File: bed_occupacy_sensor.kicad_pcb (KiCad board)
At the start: 2 copper layers, 48 x 34 mm, 6 parts, among them J1 FSR_2, J2 FSR_1, U1 mini_esp32

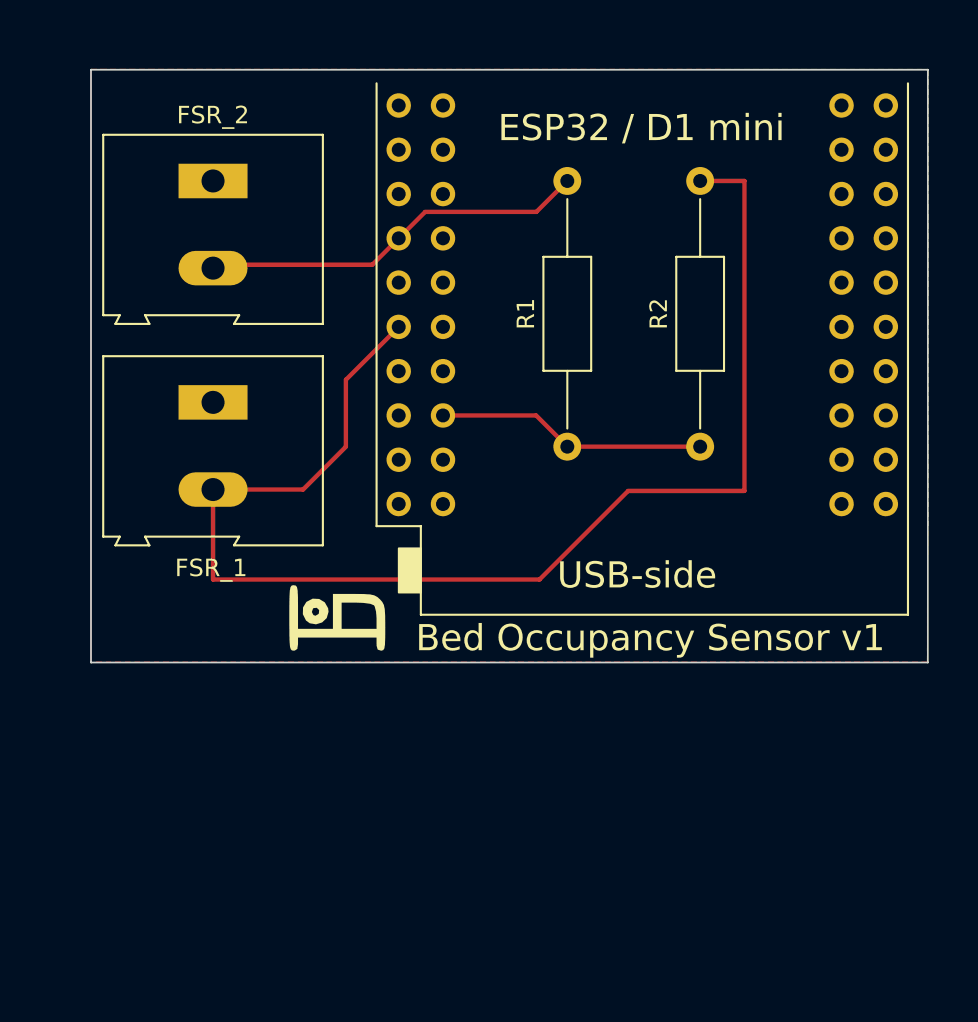
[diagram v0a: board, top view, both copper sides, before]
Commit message: Updated to design ESP32 flipped to get smaller PCB added QR-Code for Project-Link
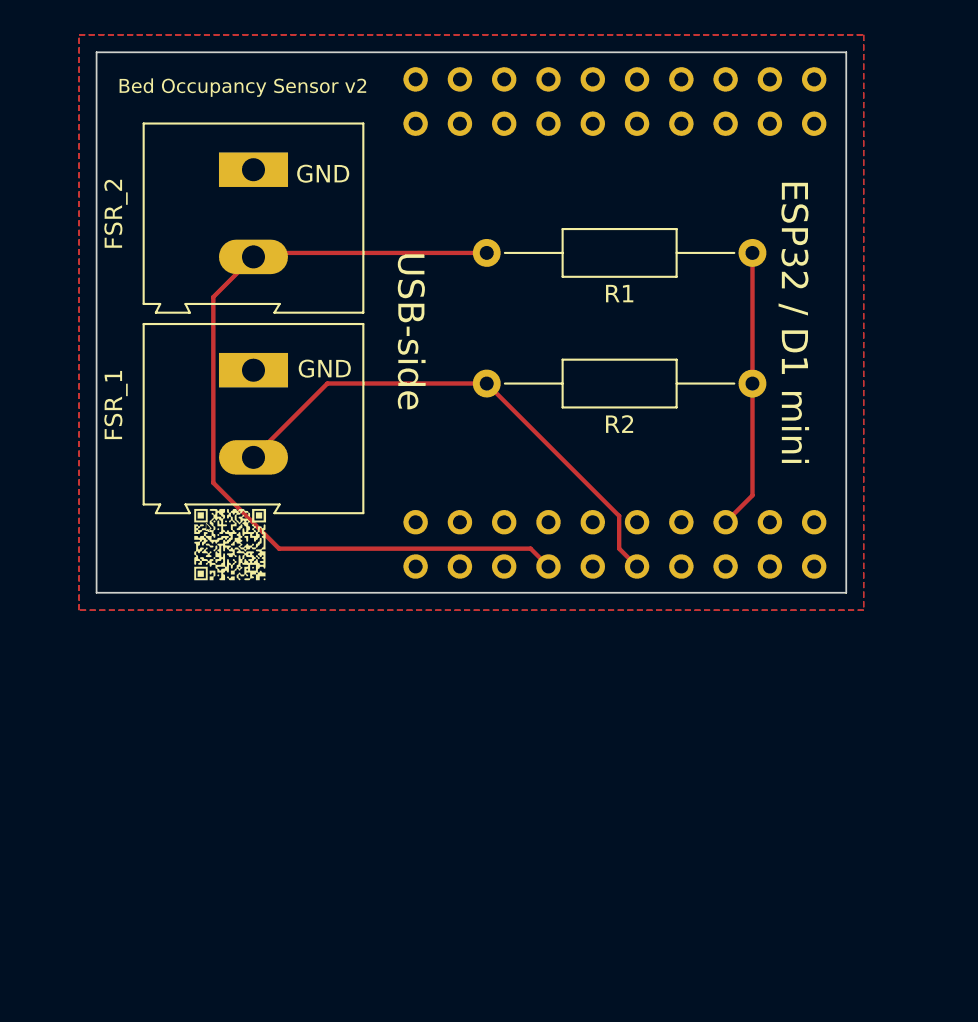
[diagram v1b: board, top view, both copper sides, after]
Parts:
- removed the G*** at (171.8, 123.3)
- added G***: LOGO, LOGO, F.Cu at (165.7, 119.2)
- moved R1 15.4 mm to (195.6, 102.5), turned to 180 degrees
- moved R2 4.70 mm to (195.6, 110.0), turned to 180 degrees
- moved J2 2.96 mm to (167.0, 109.2)
- moved J1 2.41 mm to (167.0, 97.7)
- moved U1 1.89 mm to (187.7, 106.5), turned to 90 degrees
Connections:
- net /GND renamed GND
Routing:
- net /SIDE_B: track 74.8 -> 29.2 mm
- net /SIDE_A: track 22.4 -> 48.6 mm
- net /+3V3: track 15.5 -> 16.1 mm
- added copper zone on B.Cu, net GND
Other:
- board size 48 x 34 mm -> 43 x 31 mm
- board text added: "Bed Occupancy Sensor v2"
- board text added: "GND"
- board text removed: "Bed Occupancy Sensor v1"

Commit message: complete redesign added terminal-block for getting power from external powersupply flipped esp header for getting smaller kicad_pcb added descriptions for pins and QR code
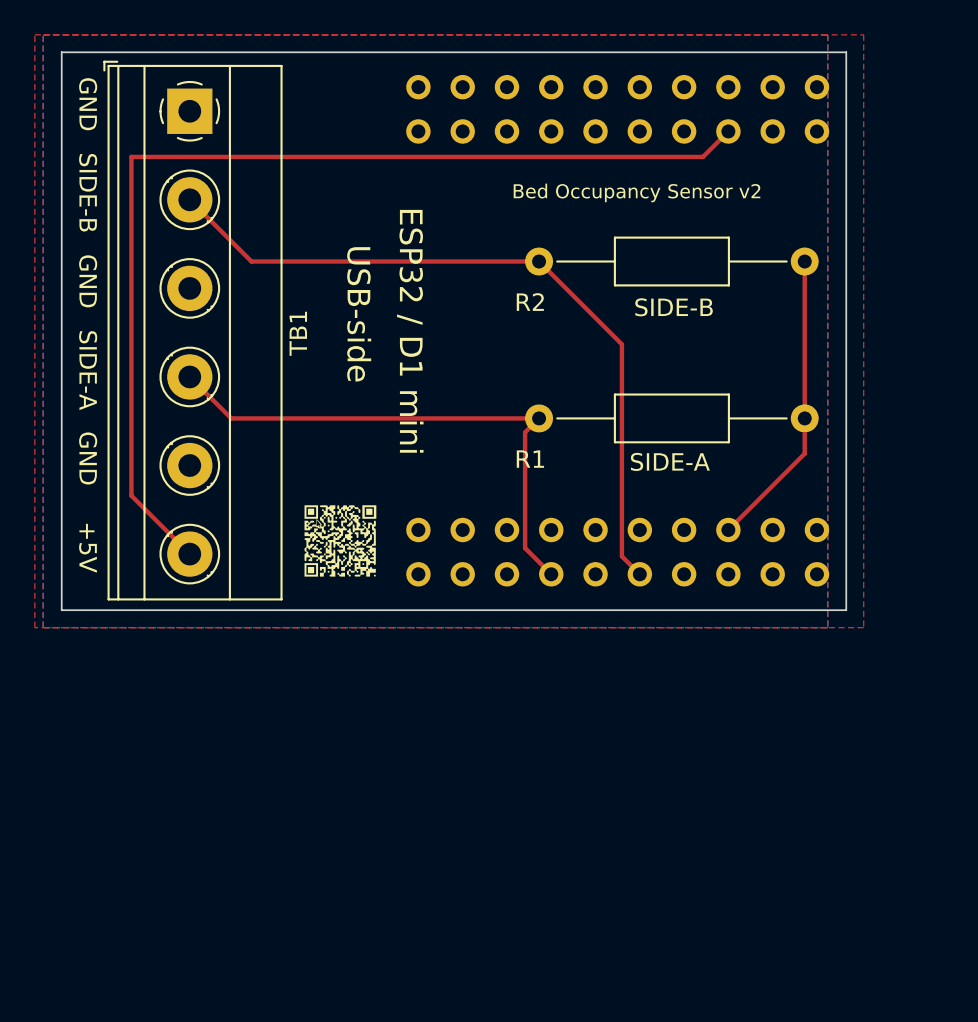
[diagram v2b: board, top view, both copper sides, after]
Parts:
- removed J1: FSR_2, TerminalBlock:TerminalBlock_Altech_AK300-2_P5.00mm
- removed J2: FSR_1, TerminalBlock:TerminalBlock_Altech_AK300-2_P5.00mm
- added TB1: 1729160, TerminalBlock_Phoenix:TerminalBlock_Phoenix_MKDS-1,5-6-5.08_1x06_P5.08mm_Horizontal, F.Cu at (163.3, 94.4)
- moved R1 9.96 mm to (198.6, 112.0)
- moved R2 7.62 mm to (198.6, 103.0)
- moved G*** 6.33 mm to (172.0, 119.0)
- moved U1 0.47 mm to (187.9, 107.0)
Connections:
- U1 pad 1: GND -> unconnected-(U1-Pad1)
- U1 pad 33: GND -> unconnected-(U1-Pad33)
- U1 pad 35: unconnected-(U1-Pad35) -> /VCC
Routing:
- net /VCC: track 0.00 -> 59.0 mm
- net /SIDE_A: track 48.6 -> 30.9 mm
- net /SIDE_B: track 29.2 -> 41.8 mm
- net /+3V3: track 16.1 -> 17.2 mm
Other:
- board size 43 x 31 mm -> 45 x 32 mm
- board text added: "+5V"
- board text added: "SIDE-A"
- board text added: "SIDE-B"

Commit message: Reverse the footprint of ESP, as it was the wrong way around
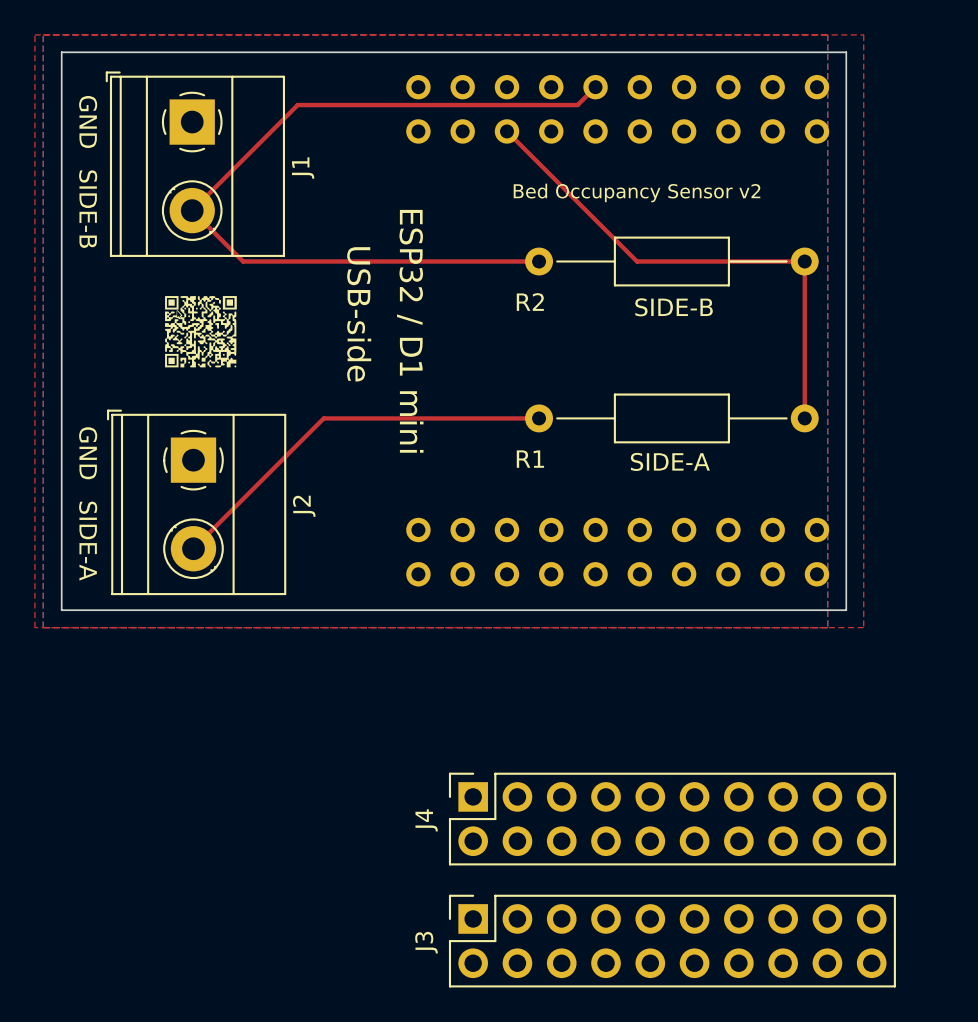
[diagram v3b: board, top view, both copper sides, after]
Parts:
- removed TB1: 1729160, TerminalBlock_Phoenix:TerminalBlock_Phoenix_MKDS-1,5-6-5.08_1x06_P5.08mm_Horizontal
- added J1: Screw_Terminal_01x02, TerminalBlock_Phoenix:TerminalBlock_Phoenix_MKDS-1,5-2-5.08_1x02_P5.08mm_Horizontal, F.Cu at (163.5, 95.0)
- added J2: Screw_Terminal_01x02, TerminalBlock_Phoenix:TerminalBlock_Phoenix_MKDS-1,5-2-5.08_1x02_P5.08mm_Horizontal, F.Cu at (163.6, 114.4)
- added J3: Conn_02x10_Top_Bottom, Connector_PinSocket_2.54mm:PinSocket_2x10_P2.54mm_Vertical, F.Cu at (179.6, 140.7)
- added J4: Conn_02x10_Top_Bottom, Connector_PinSocket_2.54mm:PinSocket_2x10_P2.54mm_Vertical, F.Cu at (179.6, 133.7)
- moved G*** 14.4 mm to (164.0, 107.0)
- turned U1 to -90 degrees
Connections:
- net /+3V3 renamed Net-(R1-Pad1)
- U1 pad 35: /VCC -> unconnected-(U1-Pad35)
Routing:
- net /VCC: track 59.0 -> 0.00 mm
- net Net-(R1-Pad1): track 17.2 -> 29.2 mm
- net /SIDE_A: track 30.9 -> 22.9 mm
- net /SIDE_B: track 41.8 -> 47.2 mm
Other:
- board text removed: "+5V"

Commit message: fixed design flaw of ESP-Pin orientation (it was the wrong way around). Now the antenna is free (on it's downside) removed QR Code because it's too small to read by a QR-Code-Reader. Updated the resistor footprint to a smaller one (10,4mm) because it fits better to standard metal-film resistors
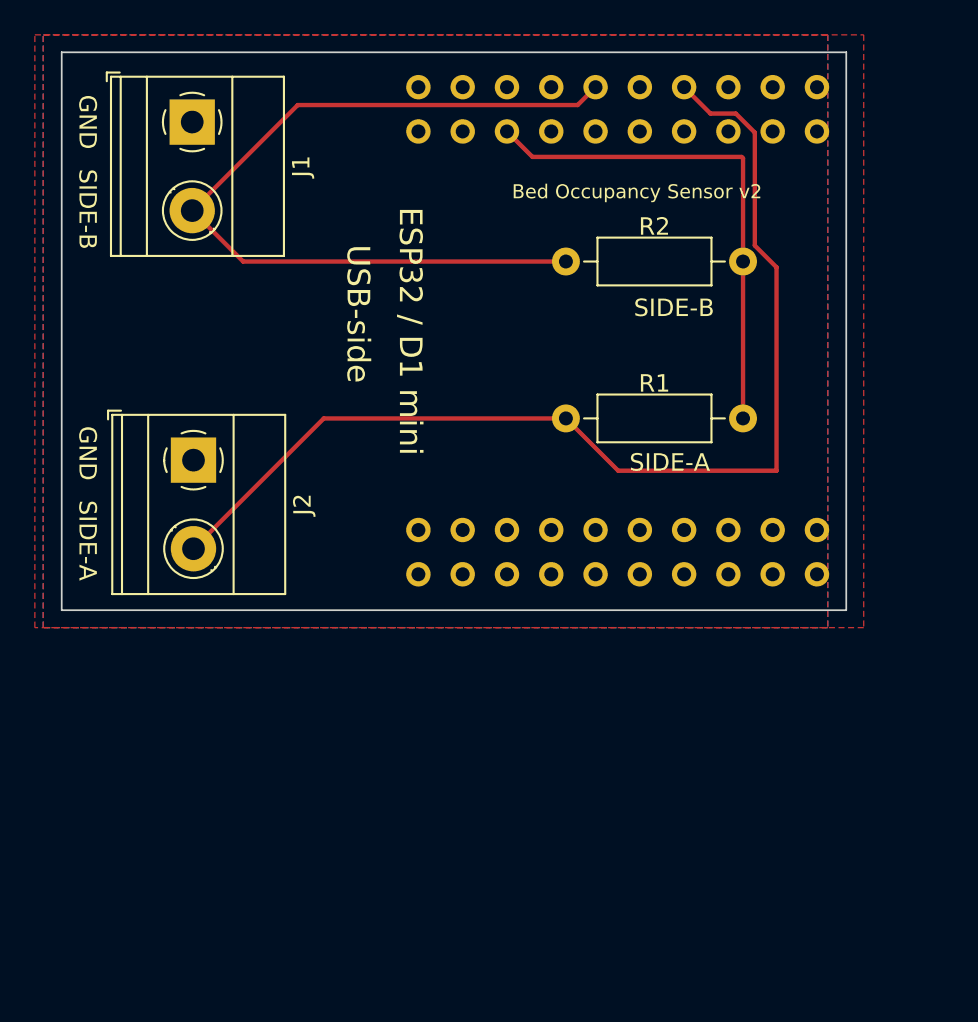
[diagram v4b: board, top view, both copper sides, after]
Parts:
- removed G***: LOGO, LOGO
- removed J3, J4: Conn_02x10_Top_Bottom, Connector_PinSocket_2.54mm:PinSocket_2x10_P2.54mm_Vertical
- R1, R2: footprint Resistor_THT:R_Axial_DIN0207_L6.3mm_D2.5mm_P15.24mm_Horizontal -> Resistor_THT:R_Axial_DIN0207_L6.3mm_D2.5mm_P10.16mm_Horizontal
- moved R1 3.54 mm to (195.1, 112.0)
- moved R2 3.54 mm to (195.1, 103.0)
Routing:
- net /SIDE_A: track 22.9 -> 62.8 mm
- net /SIDE_B: track 47.2 -> 48.7 mm

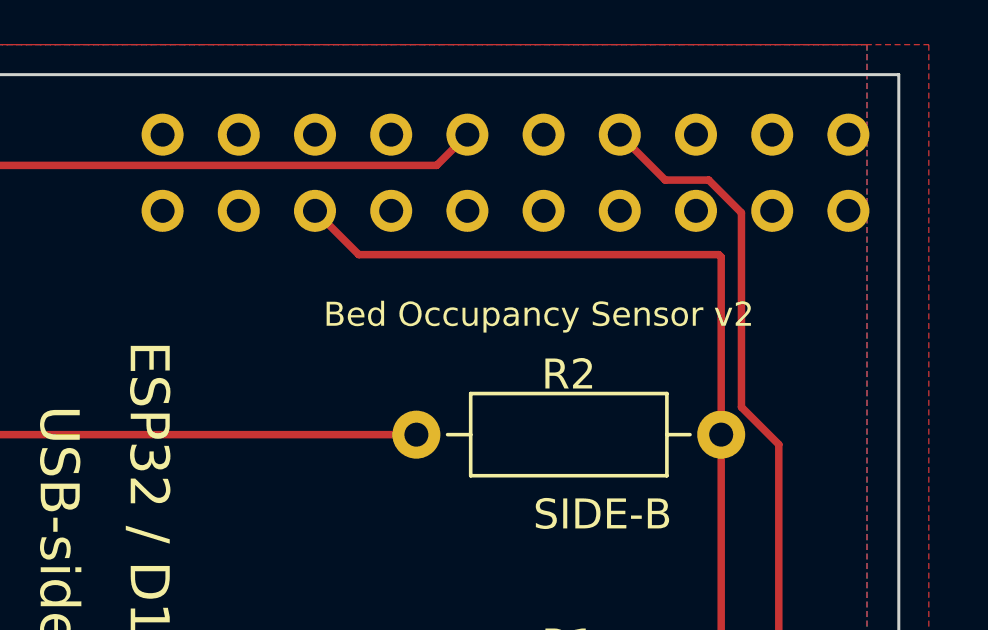
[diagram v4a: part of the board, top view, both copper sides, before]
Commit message: changed text on silkscreen to v3 reflecting changes in schematic
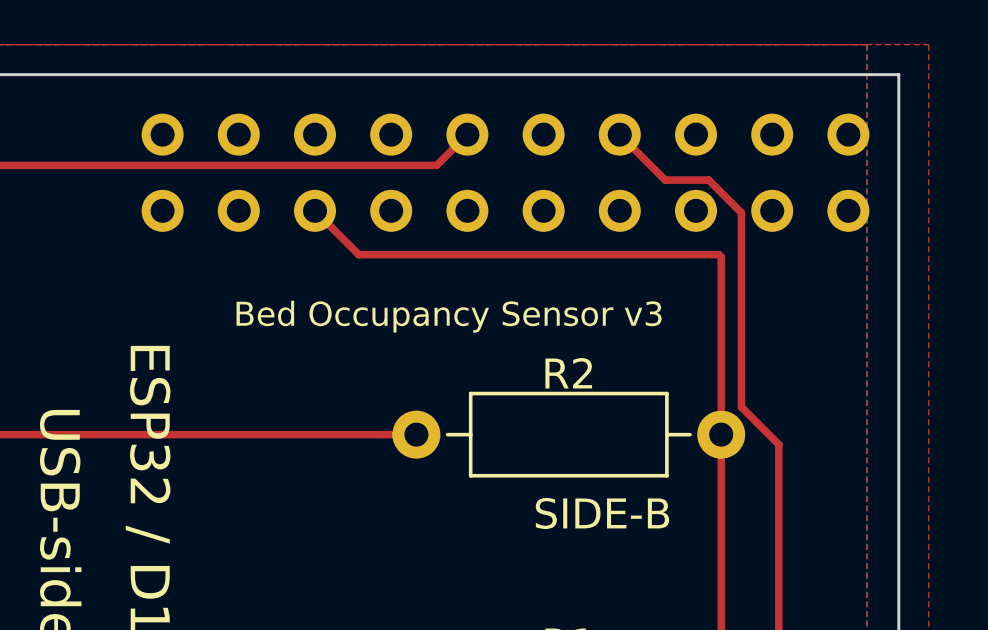
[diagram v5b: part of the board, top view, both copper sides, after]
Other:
- board text added: "Bed Occupancy Sensor v3"
- board text removed: "Bed Occupancy Sensor v2"
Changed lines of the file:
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@@
     (effects (font (size 1 1) (thickness 0.15)))
   )
-  (gr_text "Bed Occupancy Sensor v2" (at 189 99) (layer "F.SilkS")
+  (gr_text "Bed Occupancy Sensor v3" (at 186 99) (layer "F.SilkS")
     (effects (font (size 0.8 0.8) (thickness 0.15)))
   )
@@
     (pts (xy 155.46 91) (xy 155.46 123))
     (height 3)
-    (gr_text "32,0000 mm" (at 149.86 106.68 90) (layer "F.Cu")
+    (gr_text "32.0000 mm" (at 149.86 106.68 90) (layer "F.Cu")
       (effects (font (size 1.5 1.5) (thickness 0.3)))
     )
@@
     (pts (xy 156 91) (xy 201 91))
     (height -4)
-    (gr_text "45,0000 mm" (at 178.5 85.2) (layer "F.Cu")
+    (gr_text "45.0000 mm" (at 178.5 85.2) (layer "F.Cu")
       (effects (font (size 1.5 1.5) (thickness 0.3)))
     )
